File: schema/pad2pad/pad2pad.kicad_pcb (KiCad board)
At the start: 2 copper layers, 15.5 x 7.8 mm, 2 parts, among them J1 Conn_01x01_Male, J2 Conn_01x01_Male

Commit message: ardrill command, pad2pad&soic projects
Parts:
- removed J2: Conn_01x01_Male, Connector_Wire:SolderWirePad_1x01_SMD_1x2mm
- added D1: LED, LED_SMD:LED_0805_2012Metric, F.Cu at (2.54, -7.62)
- added R1: R, Resistor_SMD:R_0805_2012Metric, F.Cu at (7.62, -7.64)
- J1: value Conn_01x01_Male -> Conn_01x02_Male; footprint Connector_Wire:SolderWirePad_1x01_SMD_1x2mm -> Connector_PinHeader_2.54mm:PinHeader_1x02_P2.54mm_Vertical
- moved J1 11.8 mm to (2.54, -2.54)
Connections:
- J1 pad 1: Net-(J1-Pad1) -> +5V
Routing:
- net Net-(J1-Pad1): track 7.71 -> 0.00 mm
- net GND: track 0.00 -> 7.36 mm
- net +5V: track 0.00 -> 5.22 mm
- net Net-(D1-Pad1): track 0.00 -> 2.97 mm
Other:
- board size 15.5 x 7.8 mm -> 10.2 x 10.2 mm

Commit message: alignment edges fixed
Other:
- board size 10.2 x 10.2 mm -> 10 x 10 mm
- board text added: "pad 1x2mm trk 0.5 mm"
- board text removed: "pad 1x2mm track 0.5 mm"

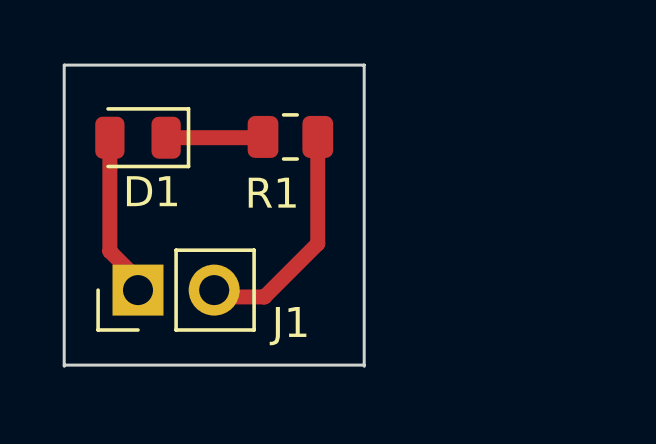
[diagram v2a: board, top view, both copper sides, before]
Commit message: fixed example: pad2pad, dip, added: milldrill option
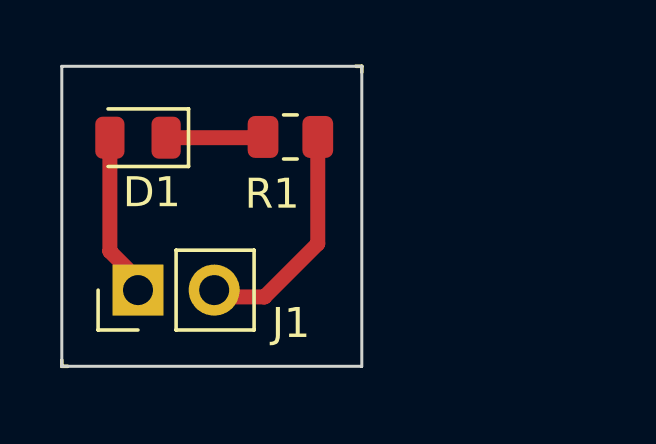
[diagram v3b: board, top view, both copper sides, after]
